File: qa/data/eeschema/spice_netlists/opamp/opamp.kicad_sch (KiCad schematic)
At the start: 6 parts, among them U1 OPAMP

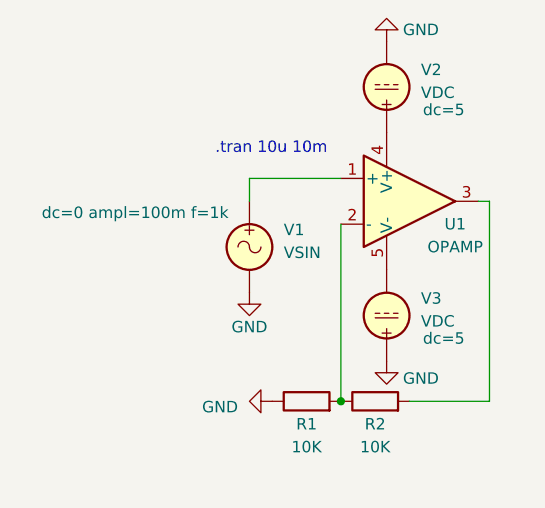
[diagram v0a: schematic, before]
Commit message: Hide voltage/current source param-value pair if value is 0
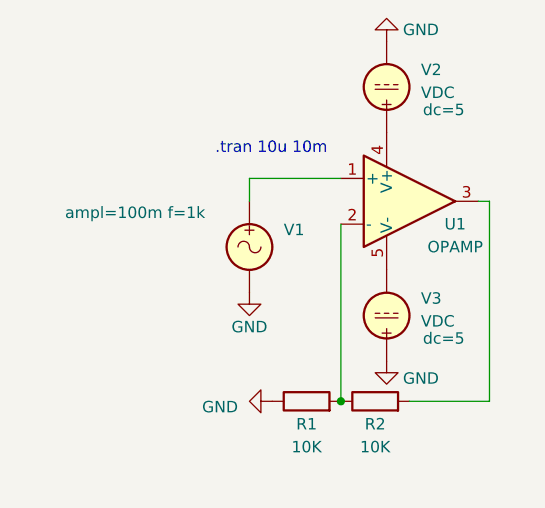
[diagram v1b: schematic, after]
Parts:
- V1: value VSIN -> (none); Model_Params dc=0 ampl=100m f=1k -> ampl=100m f=1k
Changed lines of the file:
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@@
       (effects (font (size 1.27 1.27)) (justify left))
     )
-    (property "Value" "VSIN" (id 1) (at 146.05 97.155 0)
+    (property "Value" "" (id 1) (at 146.05 97.155 0)
       (effects (font (size 1.27 1.27)) (justify left))
     )
@@
       (effects (font (size 1.27 1.27)) hide)
     )
-    (property "Model_Params" "dc=0 ampl=100m f=1k" (id 7) (at 129.54 92.71 0)
+    (property "Model_Params" "ampl=100m f=1k" (id 7) (at 129.54 92.71 0)
       (effects (font (size 1.27 1.27)))
     )

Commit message: Infer models for voltage and current sources
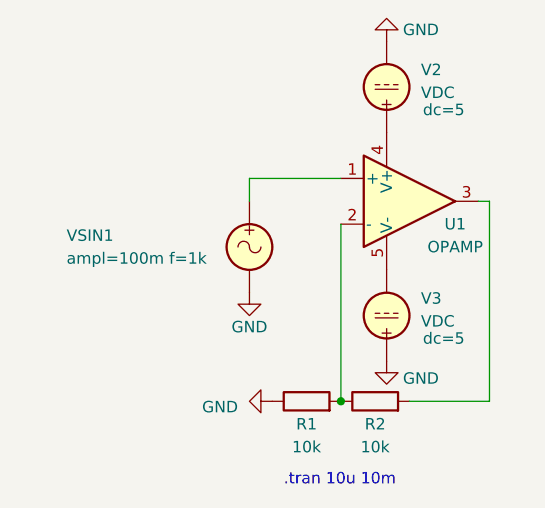
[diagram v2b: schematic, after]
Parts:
- R1, R2: value 10K -> 10k
- VSIN1: renamed from V1; value (none) -> ampl=100m f=1k; Model_Device V -> (none); Model_Params ampl=100m f=1k -> (none); Model_Pins 1 2 -> (none); Model_Type SIN -> (none)
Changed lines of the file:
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@@
     (stroke (width 0) (type default))
   )
-  (text ".tran 10u 10m" (at 138.43 86.36 0)
+  (text ".tran 10u 10m" (at 146.05 123.19 0)
     (effects (font (size 1.27 1.27)) (justify left bottom))
   )
@@
   (symbol (lib_id "Simulation_SPICE:VSIN") (at 142.24 96.52 0) (unit 1)
     (in_bom yes) (on_board yes)
-    (property "Reference" "V1" (id 0) (at 146.05 94.615 0)
+    (property "Reference" "VSIN1" (id 0) (at 121.92 95.25 0)
       (effects (font (size 1.27 1.27)) (justify left))
     )
-    (property "Value" "" (id 1) (at 146.05 97.155 0)
+    (property "Value" "ampl=100m f=1k" (id 1) (at 121.92 97.79 0)
       (effects (font (size 1.27 1.27)) (justify left))
     )
@@
       (effects (font (size 1.27 1.27)) hide)
     )
-    (property "Model_Device" "V" (id 4) (at 142.24 96.52 0)
-      (effects (font (size 1.27 1.27)) hide)
-    )
-    (property "Model_Type" "SIN" (id 5) (at 142.24 96.52 0)
-      (effects (font (size 1.27 1.27)) hide)
-    )
-    (property "Model_Pins" "1 2" (id 6) (at 142.24 96.52 0)
-      (effects (font (size 1.27 1.27)) hide)
-    )
-    (property "Model_Params" "ampl=100m f=1k" (id 7) (at 129.54 92.71 0)
-      (effects (font (size 1.27 1.27)))
-    )
     (pin "1")
     (pin "2")
@@
       (effects (font (size 1.27 1.27)))
     )
-    (property "Value" "10K" (id 1) (at 156.21 118.745 90)
+    (property "Value" "10k" (id 1) (at 156.21 118.745 90)
       (effects (font (size 1.27 1.27)))
     )
@@
       (effects (font (size 1.27 1.27)))
     )
-    (property "Value" "10K" (id 1) (at 148.59 118.745 90)
+    (property "Value" "10k" (id 1) (at 148.59 118.745 90)
       (effects (font (size 1.27 1.27)))
     )
@@
     )
     (path "/fbe00ebb-3cab-46ea-988c-9e8169e9708f"
-      (reference "R1") (unit 1) (value "10K") (footprint "")
+      (reference "R1") (unit 1) (value "10k") (footprint "")
     )
     (path "/2a5b0448-42a8-4fa4-9a14-267dc34f9ff7"
-      (reference "R2") (unit 1) (value "10K") (footprint "")
+      (reference "R2") (unit 1) (value "10k") (footprint "")
     )
     (path "/3dd58d42-1028-4fbc-adf4-32d03de981a6"
       (reference "U1") (unit 1) (value "OPAMP") (footprint "")
     )
-    (path "/10f44001-5f65-44eb-a535-b7b3c67d5b83"
-      (reference "V1") (unit 1) (value "VSIN") (footprint "")
-    )
     (path "/383ea298-1cb3-473e-8fce-19d3c7ac3912"
       (reference "V2") (unit 1) (value "VDC") (footprint "")
@@
       (reference "V3") (unit 1) (value "VDC") (footprint "")
     )
-  )
+    (path "/10f44001-5f65-44eb-a535-b7b3c67d5b83"
+      (reference "VSIN1") (unit 1) (value "ampl=100m f=1k") (footprint "")
+    )
+  )

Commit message: Fix Spice netlist exporter tests
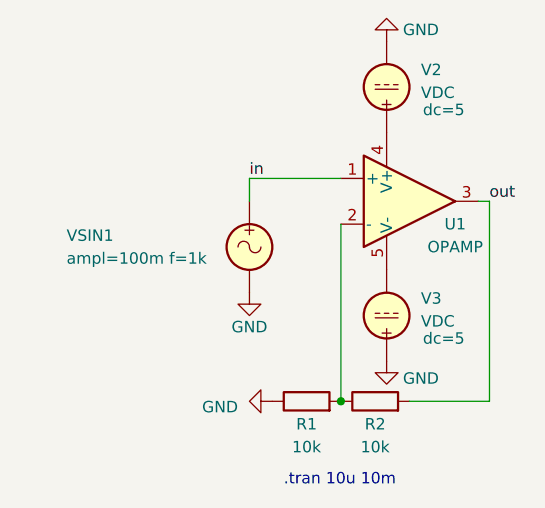
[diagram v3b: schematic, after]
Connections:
- net in: now reaches U1.1 (+), VSIN1.1
- net out: now reaches R2.2, U1.3
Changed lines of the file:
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@@
+    (effects (font (size 1.27 1.27)) (justify left bottom))
+  )
+  (label "out" (at 168.91 91.44 0) (fields_autoplaced)
+    (effects (font (size 1.27 1.27)) (justify left bottom))
+  )
+  (label "in" (at 142.24 88.9 0) (fields_autoplaced)
     (effects (font (size 1.27 1.27)) (justify left bottom))
   )

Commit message: Make sim QA tests compare result vectors, not netlist text
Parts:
- U1: Model_Library opamp.lib -> opamp.lib.spice; Model_Name uopamp_lvl2 -> uopamp_lvl1; Model_Pins 1 2 4 5 3 -> 1 2 3
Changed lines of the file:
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@@
       (effects (font (size 1.27 1.27)) hide)
     )
-    (property "Model_Name" "uopamp_lvl2" (id 6) (at 160.02 91.44 0)
+    (property "Model_Name" "uopamp_lvl1" (id 6) (at 160.02 91.44 0)
       (effects (font (size 1.27 1.27)) hide)
     )
-    (property "Model_Library" "opamp.lib" (id 7) (at 160.02 91.44 0)
+    (property "Model_Library" "opamp.lib.spice" (id 7) (at 160.02 91.44 0)
       (effects (font (size 1.27 1.27)) hide)
     )
@@
       (effects (font (size 1.27 1.27)) hide)
     )
-    (property "Model_Pins" "1 2 4 5 3" (id 9) (at 160.02 91.44 0)
+    (property "Model_Pins" "1 2 3" (id 9) (at 160.02 91.44 0)
       (effects (font (size 1.27 1.27)) hide)
     )
